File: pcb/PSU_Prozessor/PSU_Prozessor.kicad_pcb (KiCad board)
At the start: 2 copper layers, 192.4 x 77 mm, 88 parts, among them IC1 6N138S, J1 ACJS-MHOP, J2 Conn_01x06, J3 FC68148S, J4 USB2066-05-RBHM-15-STB-00-01-A, J7 USB2066-05-RBHM-15-STB-00-01-A, Q1 BC847, Q2 2N7002, Q3 BC847, Q4 2N7002, Q5 BC847, Q6 2N7002, U1 TL072, U2 TL072

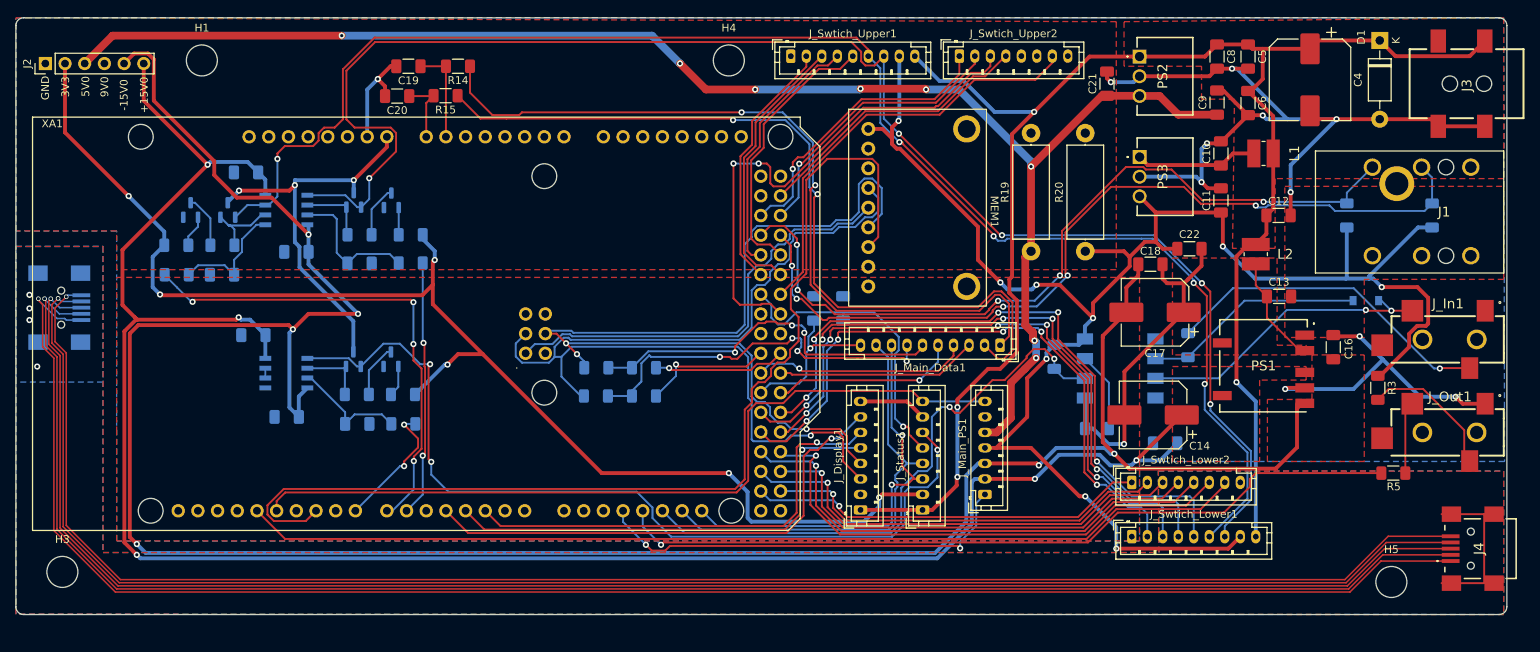
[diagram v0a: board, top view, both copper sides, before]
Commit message: New version with smaller enclosure
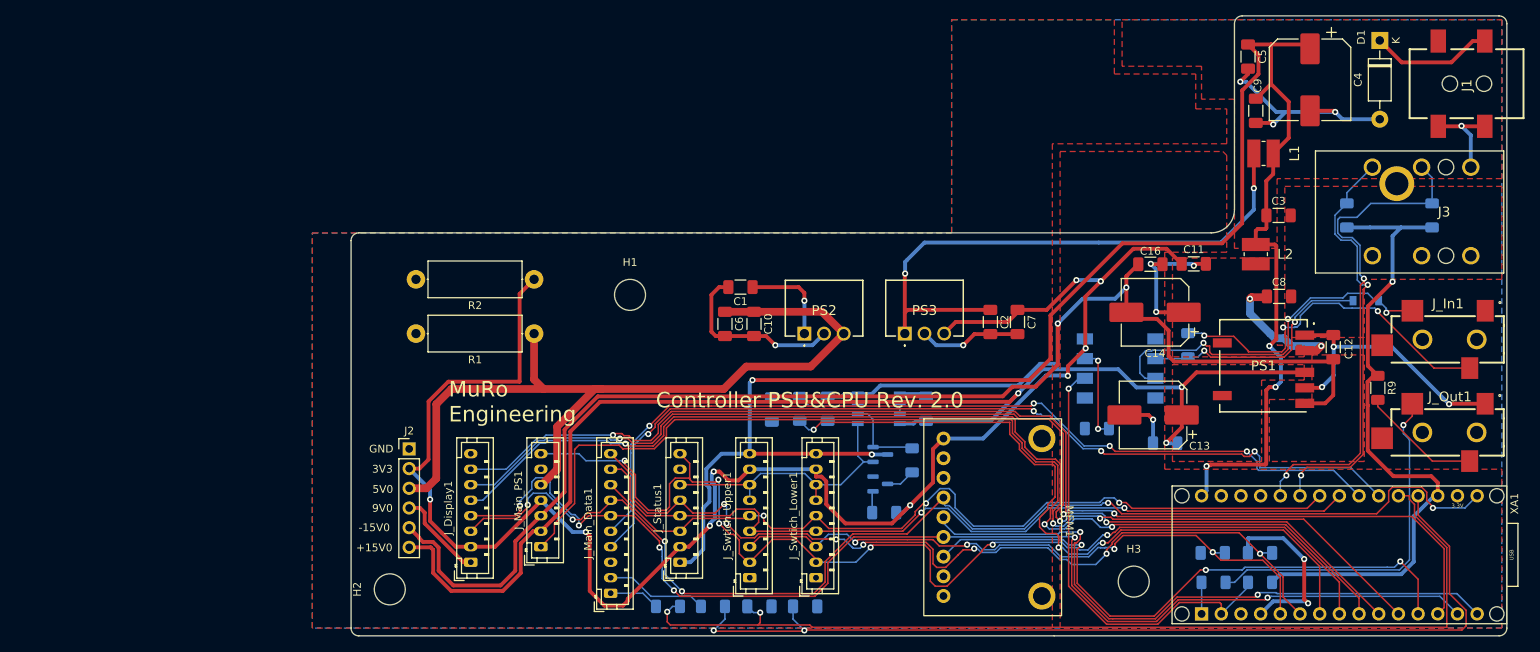
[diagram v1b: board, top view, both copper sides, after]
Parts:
- removed the C23 at (75.7, 82.5)
- removed C24, C27: 100n, Capacitor_SMD:C_1206_3216Metric_Pad1.33x1.80mm_HandSolder
- removed C25: 1u, Capacitor_SMD:C_1206_3216Metric_Pad1.33x1.80mm_HandSolder
- removed the C7 at (72.6, 95.7)
- removed H4, H5: MountingHole, KiCad_Libs:MountingHole_4mm
- removed J4, J7: USB2066-05-RBHM-15-STB-00-01-A, SamacSys_Parts:USB206605RBHM15STB0001A
- removed J_Swtich_Lower2, J_Swtich_Upper2: Conn_01x08, Connector_JST:JST_PH_B8B-PH-K_1x08_P2.00mm_Vertical
- removed Q3, Q5: BC847, Package_TO_SOT_SMD:SOT-23
- removed Q4, Q6: 2N7002, Package_TO_SOT_SMD:SOT-23
- removed R16: 33k, Resistor_SMD:R_1206_3216Metric_Pad1.30x1.75mm_HandSolder
- removed R17: 330, Resistor_SMD:R_1206_3216Metric_Pad1.30x1.75mm_HandSolder
- removed R18: 10k, Resistor_SMD:R_1206_3216Metric_Pad1.30x1.75mm_HandSolder
- removed R21, R22, R23, R24: 0, Resistor_SMD:R_1206_3216Metric_Pad1.30x1.75mm_HandSolder
- removed the R6 at (66.8, 95.7)
- removed the R7 at (72.7, 91.8)
- removed the R8 at (66.7, 91.8)
- removed U2: TL072, SamacSys_Parts:SOIC127P600X175-8N
- added C19: 100n, Capacitor_SMD:C_1206_3216Metric_Pad1.33x1.80mm_HandSolder, B.Cu at (200.4, 131.6)
- added H3: MountingHole, KiCad_Libs:MountingHole_4mm, F.Cu at (190.2, 135.2)
- C17: renamed from C19; moved to B.Cu
- C20: moved to B.Cu
- R3: renamed from R14; moved to B.Cu
- R4: renamed from R5; moved to B.Cu
- R7: renamed from R15; moved to B.Cu
- XA1: value Arduino_Due_Shield -> Arduino_Nano_Socket; footprint Arduino:Arduino_Due_Shield -> Arduino:Arduino_Nano_Socket
- moved XA1 190.2 mm to (238.4, 131.8), turned to 90 degrees
- moved C21 87.3 mm to (163.4, 113.0), turned to 90 degrees
- moved C20 84.3 mm to (147.8, 138.4), turned to 0 degrees
- moved C17 83.1 mm to (141.9, 138.4), turned to 0 degrees
- moved U1 80.6 mm to (157.3, 113.0), turned to 0 degrees
- moved R14 77.0 mm to (161.7, 119.6), turned to -90 degrees
- moved Q1 75.5 mm to (157.6, 118.8), turned to 0 degrees
- moved R3 74.8 mm to (130.2, 138.4), turned to 0 degrees
- moved R7 74.4 mm to (135.9, 138.4), turned to 0 degrees
- moved Q2 72.9 mm to (157.6, 122.7), turned to 0 degrees
- moved R2 71.2 mm to (112.9, 96.2), turned to 180 degrees
- moved R13 70.8 mm to (158.1, 126.3)
- moved C22 69.8 mm to (150.8, 113.0), turned to 90 degrees
- moved C6 69.6 mm to (137.5, 102.0), turned to -90 degrees
- moved J2 68.4 mm to (96.8, 118.1), turned to 0 degrees
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- renumbered C8 to C1, C21 to C10, C22 to C11, C16 to C12, C14 to C13, C17 to C14, C18 to C16, C26 to C18, C10 to C2, C2 to C21, C3 to C22, C1 to C23, C12 to C3, C9 to C6, C11 to C7, C13 to C8, C6 to C9, H3 to H2, J3 to J1, J1 to J3, R19 to R1, R9 to R10, R1 to R12, R4 to R13, R2 to R14, R20 to R2, R12 to R5, R13 to R6, R10 to R8, R3 to R9
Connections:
- J_Main_Data1 pad 10: /INT_Matrix -> /INT_Status
- J_Main_Data1 pad 3: /EN_SPL_Matrix -> unconnected-(J_Main_Data1-Pad3)
- J_Main_Data1 pad 6: Net-(J_Main_Data1-Pad6) -> /MOSI
- J_Main_Data1 pad 7: Net-(J_Main_Data1-Pad7) -> /SCK
- J_Status1 pad 6: /Vref_status -> /Vref_bl
- J_Swtich_Lower1 pad 2: /RCLK_Lower -> /I2C_Reset
- J_Swtich_Lower1 pad 3: /SRCLR_Lower -> /INT_Switch
- J_Swtich_Lower1 pad 4: /SRCLK_Lower -> /SDA
- J_Swtich_Lower1 pad 5: /SER_Lower -> /SCL
- J_Swtich_Lower1 pad 6: /Vref_ge -> /Vref_bl
- J_Swtich_Upper1 pad 2: /RCLK_Upper -> /I2C_Reset
- J_Swtich_Upper1 pad 3: /SRCLR_Upper -> /INT_Switch
- J_Swtich_Upper1 pad 4: /SRCLK_Upper -> /SDA
- J_Swtich_Upper1 pad 5: /SER_Upper -> /SCL
- J_Swtich_Upper1 pad 6: /Vref_ge -> /Vref_bl
- U1 pad 5: Net-(C7-Pad1) -> GND
- U1 pad 6: Net-(Q3-Pad2) -> Net-(U1-Pad6)
- U1 pad 7: /Vref_ge -> Net-(U1-Pad6)
- XA1 pad A2: unconnected-(XA1-PadA2) -> /RCLK_MATRIX
- XA1 pad A3: unconnected-(XA1-PadA3) -> /SEL_Matrix
- XA1 pad A4: unconnected-(XA1-PadA4) -> /SDA
- XA1 pad A5: unconnected-(XA1-PadA5) -> /SCL
- XA1 pad A6: unconnected-(XA1-PadA6) -> /SW_Ext1
- XA1 pad A7: unconnected-(XA1-PadA7) -> /SW_Ext2
- XA1 pad AREF: unconnected-(XA1-PadAREF) -> /VDD3V3
- XA1 pad D0: unconnected-(XA1-PadD0) -> /MidiIn
- XA1 pad D1: unconnected-(XA1-PadD1) -> /MidiOut
- XA1 pad D10: /CS_Fram -> /CS_Display
- XA1 pad D11: unconnected-(XA1-PadD11) -> /MOSI
- XA1 pad D12: /I2C_Reset -> /MISO
- XA1 pad D13: /OE_Lower -> /SCK
- XA1 pad D2: /Reset_Display -> /INT_Switch
- XA1 pad D3: /ID_Select_Display -> /INT_Status
- XA1 pad D4: /CS_Display -> /Vref_bl_pwm
- XA1 pad D5: unconnected-(XA1-PadD5) -> /I2C_Reset
- XA1 pad D6: /Vref_bl_pwm -> /CS_Amp_N
- XA1 pad D7: /Vref_ge_pwm -> /Reset_Display
- XA1 pad D8: /Vref_status_pwm -> /ID_Select_Display
- XA1 pad D9: unconnected-(XA1-PadD9) -> /CS_Fram
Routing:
- net /USB1: track 222.7 -> 0.00 mm, vias 1 -> 0
- net /USB2: track 220.9 -> 0.00 mm, vias 1 -> 0
- net /USB3: track 219.2 -> 0.00 mm, vias 1 -> 0
- net /USB4: track 217.8 -> 0.00 mm, vias 1 -> 0
- net /USB5: track 216.6 -> 0.00 mm, vias 1 -> 0
- net /Vref_ge: track 196.8 -> 0.00 mm, vias 5 -> 0
- net /Vref_bl: track 200.4 -> 36.6 mm, vias 5 -> 0
- net /OE_Lower: track 129.3 -> 0.00 mm
- net /VSS15V0: track 322.4 -> 205.2 mm, vias 6 -> 2
- net /Expr_2: track 12.4 -> 128.2 mm, vias 0 -> 2
- net /Expr_1: track 8.78 -> 124.2 mm, vias 0 -> 2
- net /Vref_status: track 114.7 -> 0.00 mm, vias 3 -> 0
- net /MidiOut: track 102.7 -> 4.06 mm, vias 1 -> 0
- net /Expr_2_In: track 103.6 -> 6.55 mm, vias 2 -> 0
- net /Expr_1_In: track 106.0 -> 13.2 mm, vias 2 -> 0
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- removed copper zone on B.Cu, net /USB_Outer
- removed copper zone on F.Cu, net /USB_Outer
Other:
- board size 192.4 x 77 mm -> 149.2 x 80 mm

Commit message: All drill holes added
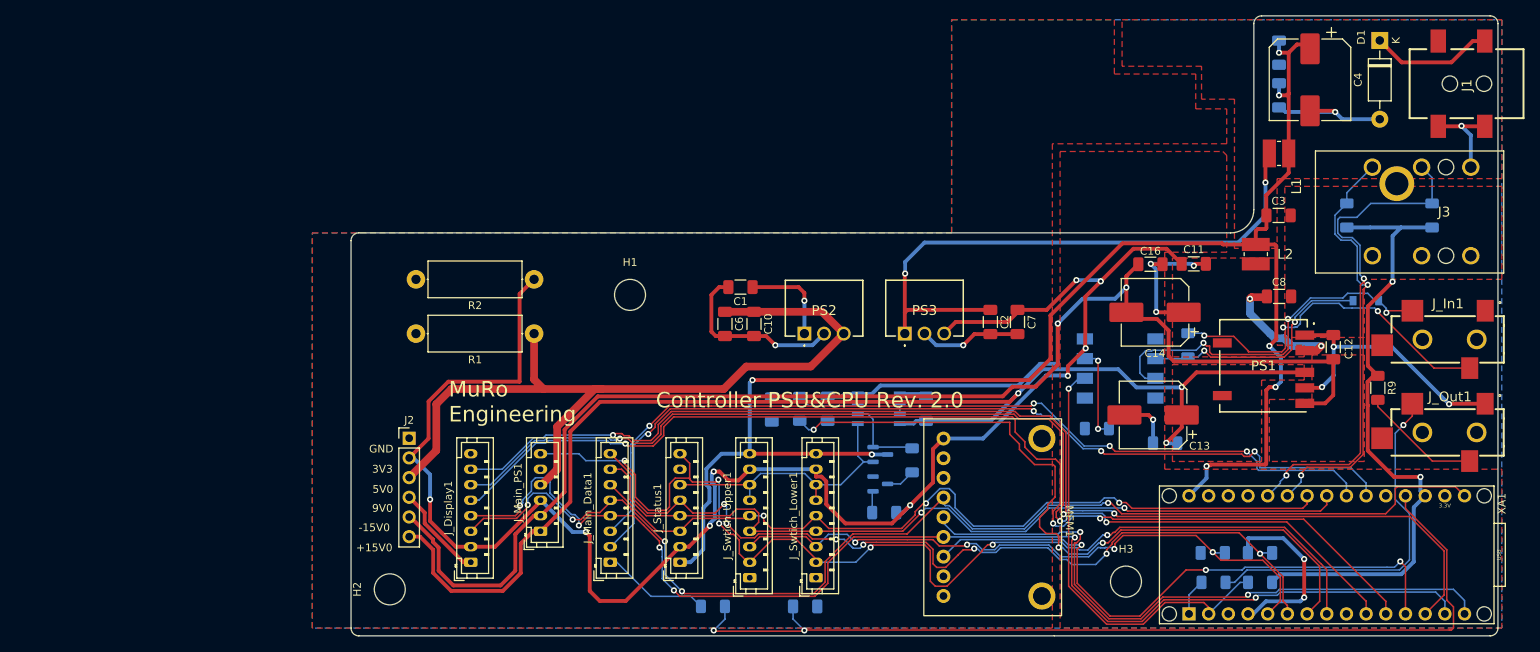
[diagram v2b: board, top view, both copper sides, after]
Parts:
- removed C17: 100n, Capacitor_SMD:C_1206_3216Metric_Pad1.33x1.80mm_HandSolder
- removed R3: 1k, Resistor_SMD:R_1206_3216Metric_Pad1.30x1.75mm_HandSolder
- C5, C9: moved to B.Cu
- J_Main_Data1: value Conn_01x10 -> Conn_01x08; footprint Connector_JST:JST_PH_B10B-PH-K_1x10_P2.00mm_Vertical -> Connector_JST:JST_PH_B8B-PH-K_1x08_P2.00mm_Vertical
- J_Main_PS1: value Conn_01x07 -> Conn_01x06; footprint Connector_JST:JST_PH_B7B-PH-K_1x07_P2.00mm_Vertical -> Connector_JST:JST_PH_B6B-PH-K_1x06_P2.00mm_Vertical
- moved C5 4.03 mm to (209.0, 67.0)
- moved J_Main_Data1 4.00 mm to (122.7, 132.8)
- moved C9 3.61 mm to (209.0, 72.5)
- moved J_Main_PS1 2.00 mm to (113.7, 128.8)
- moved L1 2.00 mm to (209.0, 80.0)
- moved XA1 1.63 mm to (236.8, 131.8)
- moved J2 1.38 mm to (96.8, 116.8)
- moved H3 1.00 mm to (189.2, 135.2)
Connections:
- J_Main_Data1 pad 1: /Expr_2_In -> /Expr_1_In
- J_Main_Data1 pad 2: /Expr_1_In -> /RCLK_MATRIX
- J_Main_Data1 pad 3: unconnected-(J_Main_Data1-Pad3) -> /SEL_Matrix
- J_Main_Data1 pad 4: /RCLK_MATRIX -> /MOSI
- J_Main_Data1 pad 5: /SEL_Matrix -> /SCK
- J_Main_Data1 pad 6: /MOSI -> /SCL
- J_Main_Data1 pad 7: /SCK -> /SDA
- J_Main_Data1 pad 8: /SCL -> /INT_Status
- J_Main_PS1 pad 1: /CS_Amp_N -> /VDD15V0
- J_Main_PS1 pad 2: /VDD15V0 -> /VSS15V0
- J_Main_PS1 pad 3: /VSS15V0 -> /VDD3V3
- J_Main_PS1 pad 4: /VDD3V3 -> /VDD5V0
- J_Main_PS1 pad 5: /VDD5V0 -> GND
- J_Main_PS1 pad 6: GND -> /I2C_Reset
- XA1 pad A1: /Expr_2 -> unconnected-(XA1-PadA1)
- XA1 pad D6: /CS_Amp_N -> unconnected-(XA1-PadD6)
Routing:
- net /CS_Amp_N: track 139.4 -> 0.00 mm, vias 2 -> 0
- net /Expr_2: track 128.2 -> 0.00 mm, vias 2 -> 0
- net /VDD9V0: track 271.8 -> 245.5 mm, vias 6 -> 8
- net GND: track 166.2 -> 153.4 mm, vias 15 -> 13
- net /Expr_2_In: track 6.55 -> 0.00 mm
- net /SCK: track 157.1 -> 153.8 mm, vias 6 -> 5
- net /VDD3V3: track 306.5 -> 303.4 mm, vias 10 -> 11
- net /VDD5V0: track 110.2 -> 107.5 mm
- net Net-(C2-Pad1): track 75.5 -> 77.6 mm
- net /Expr_1: track 124.2 -> 122.7 mm
- net /VSS15V0: track 205.2 -> 206.5 mm
- net /SCL: track 105.0 -> 104.0 mm
- net /SDA: track 107.4 -> 106.4 mm
- net /Expr_1_In: track 13.2 -> 14.1 mm
- net Net-(J_Out1-Pad2): track 45.9 -> 46.8 mm
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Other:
- board size 149.2 x 80 mm -> 148 x 80 mm
